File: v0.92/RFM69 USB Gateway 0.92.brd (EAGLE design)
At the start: 56.1 x 17 mm, 25 parts, among them IC3 MCP1703-3.3V, J1 USBPCB_NOPASTE, U1 RFM69HCW, U2 ATMEGA328P-MU, X1 16 MHz

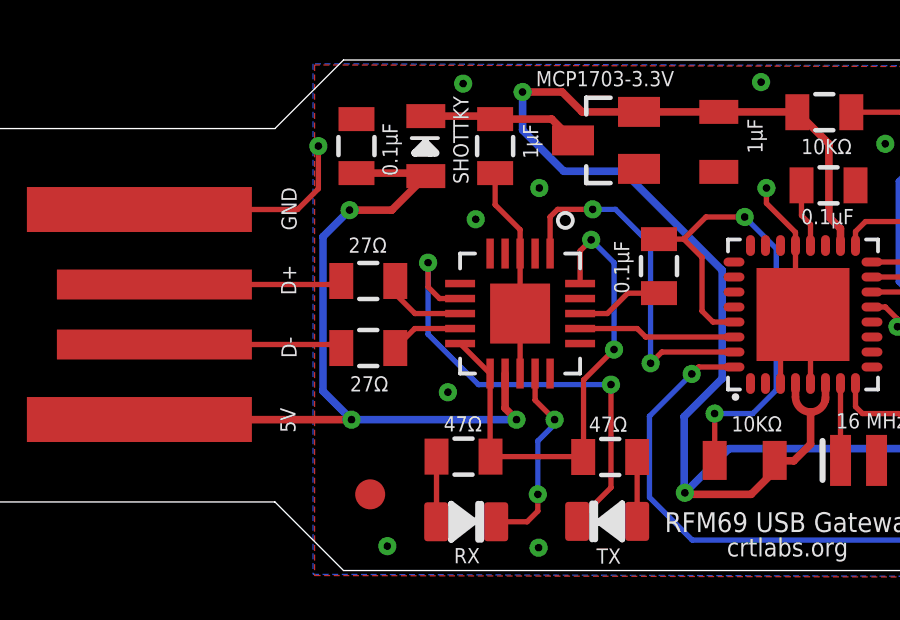
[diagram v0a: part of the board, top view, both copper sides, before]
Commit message: Relocated a via
for better silkscreen
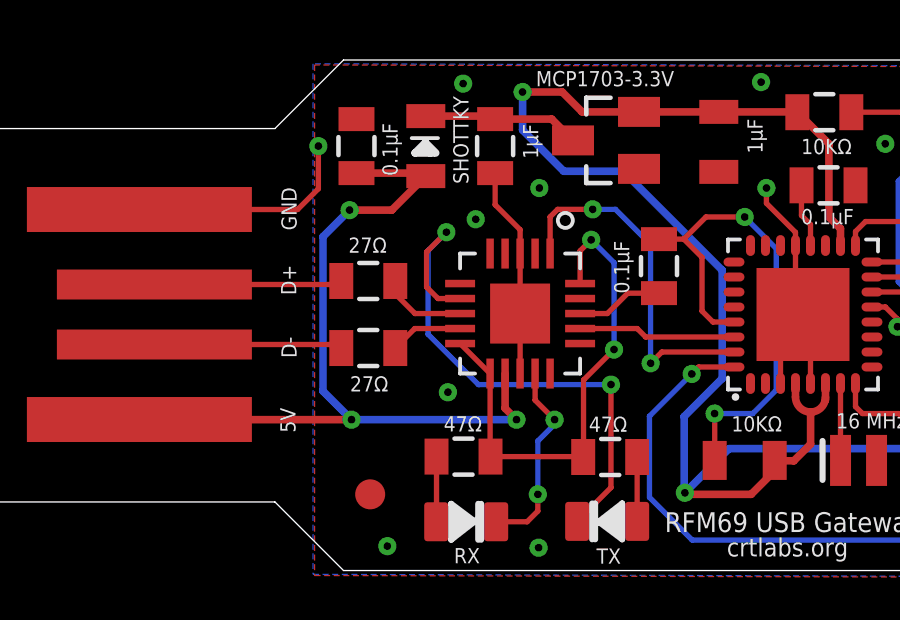
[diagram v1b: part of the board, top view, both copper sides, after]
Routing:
- net N$7: track 16.2 -> 18.9 mm
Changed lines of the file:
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@@
 <contactref element="TX" pad="MINUS"/>
 <contactref element="FT231XQ-R" pad="CBUS2"/>
-<wire x1="23.8252" y1="12.1144" x2="23.1408" y2="12.1144" width="0.1778" layer="1"/>
-<wire x1="23.1408" y1="12.1144" x2="22.7584" y2="12.4968" width="0.1778" layer="1"/>
-<wire x1="22.7584" y1="12.4968" x2="22.7584" y2="13.3096" width="0.1778" layer="1"/>
-<via x="22.7584" y="13.3096" extent="1-16" drill="0.254" diameter="0.127"/>
-<wire x1="22.7584" y1="13.3096" x2="22.7584" y2="10.922" width="0.1778" layer="16"/>
-<wire x1="22.7584" y1="10.922" x2="24.4348" y2="9.2456" width="0.1778" layer="16"/>
+<via x="23.368" y="14.3256" extent="1-16" drill="0.254" diameter="0.127"/>
+<wire x1="24.4348" y1="9.2456" x2="22.7584" y2="10.922" width="0.1778" layer="16"/>
 <wire x1="24.4348" y1="9.2456" x2="28.8544" y2="9.2456" width="0.1778" layer="16"/>
 <via x="28.8544" y="9.2456" extent="1-16" drill="0.254" diameter="0.127"/>
 <wire x1="28.8544" y1="5.8133" x2="27.7274" y2="4.6863" width="0.1778" layer="1"/>
 <wire x1="28.8544" y1="9.2456" x2="28.8544" y2="5.8133" width="0.1778" layer="1"/>
+<wire x1="23.09" y1="12.1144" x2="22.7076" y2="12.4968" width="0.1778" layer="1"/>
+<wire x1="22.7076" y1="12.4968" x2="22.7076" y2="13.6652" width="0.1778" layer="1"/>
+<wire x1="22.7076" y1="13.6652" x2="23.368" y2="14.3256" width="0.1778" layer="1"/>
+<wire x1="23.8252" y1="12.1144" x2="23.09" y2="12.1144" width="0.1778" layer="1"/>
+<wire x1="22.7584" y1="10.922" x2="22.7584" y2="13.716" width="0.1778" layer="16"/>
+<wire x1="22.7584" y1="13.716" x2="23.368" y2="14.3256" width="0.1778" layer="16"/>
 </signal>
 <signal name="N$8">
